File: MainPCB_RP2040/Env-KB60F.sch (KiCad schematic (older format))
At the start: 188 parts, among them J1 SKRKAEE020, J2 SKRKAEE020, J5 Conn_01x03_Male, U1 TLV75533PDBVR, U3 RP2040, Y1 3225_4P

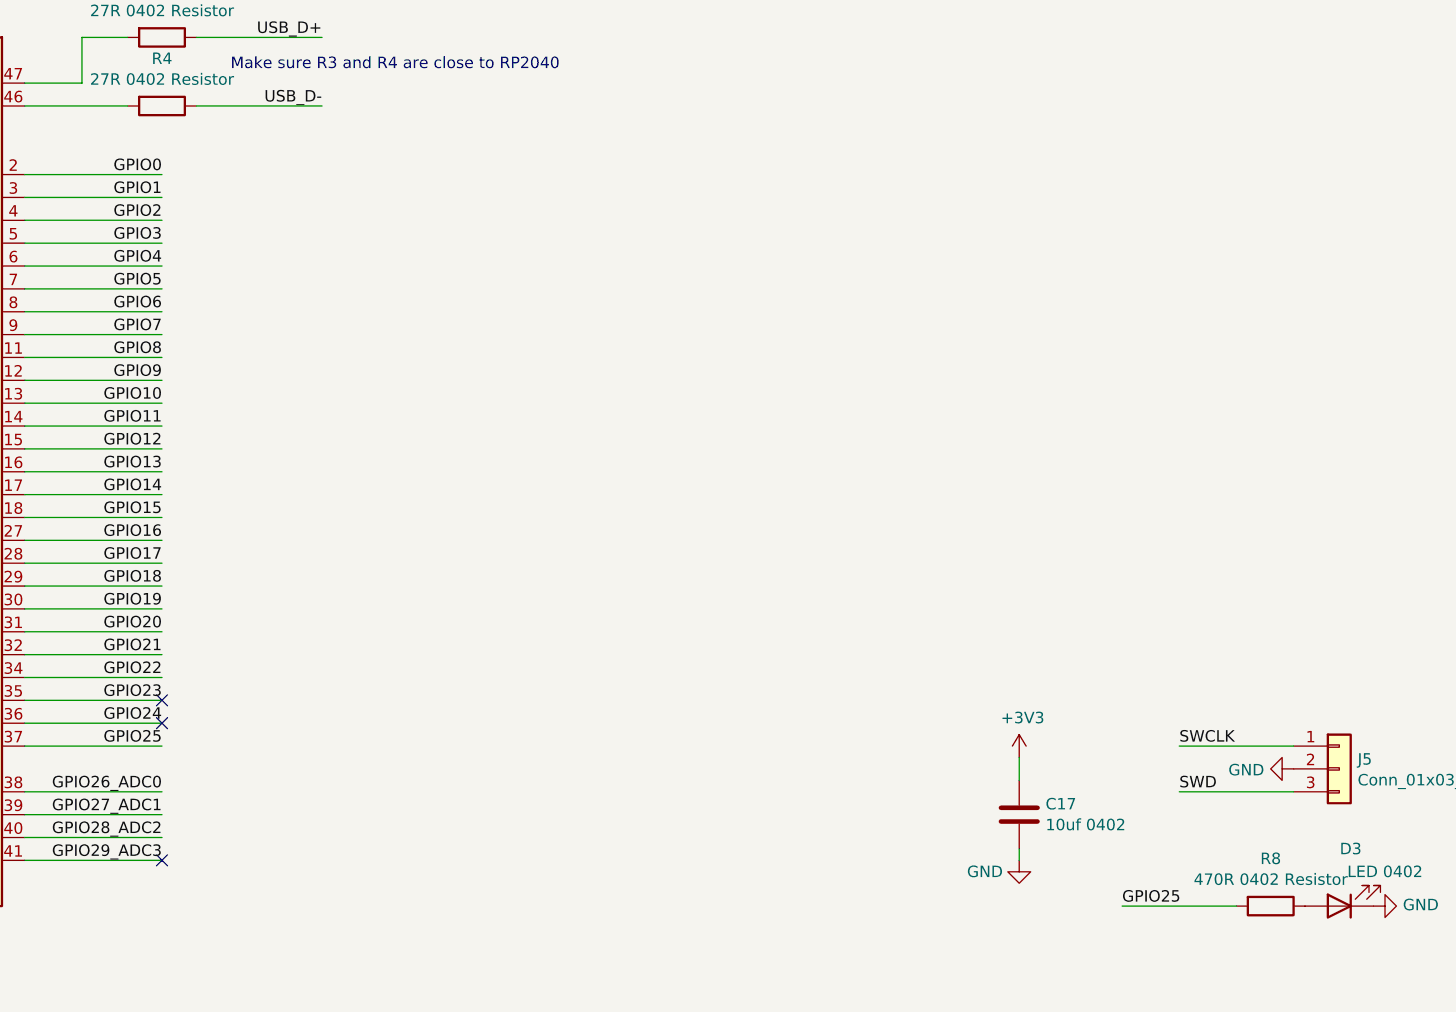
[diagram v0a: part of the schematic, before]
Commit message: finished up RP2040 version some more, added debug header and spare GPIO header.
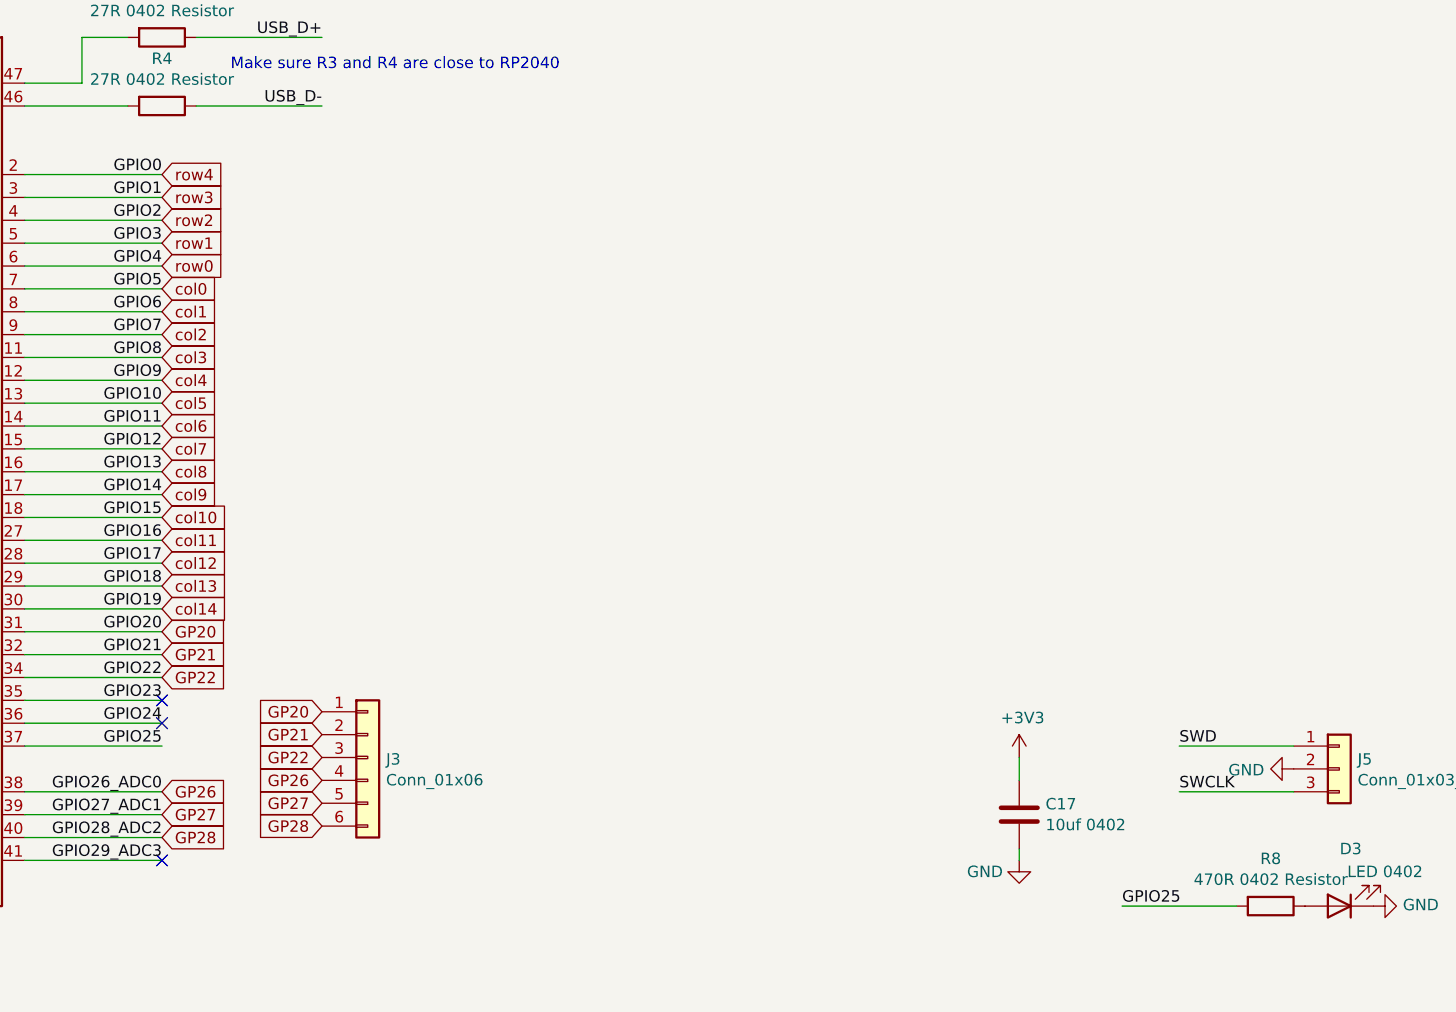
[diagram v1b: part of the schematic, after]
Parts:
- added J3: Conn_01x06, Connector_PinSocket_2.54mm:PinSocket_1x06_P2.54mm_Vertical, symbol Connector_Generic:Conn_01x06
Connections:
- net GPIO0 is gone; now on net row4: U3.2 (GPIO0)
- net GPIO1 is gone; now on net row3: U3.3 (GPIO1)
- net GPIO10 is gone; now on net col5: U3.13 (GPIO10)
- net GPIO11 is gone; now on net col6: U3.14 (GPIO11)
- net GPIO12 is gone; now on net col7: U3.15 (GPIO12)
- net GPIO13 is gone; now on net col8: U3.16 (GPIO13)
- net GPIO14 is gone; now on net col9: U3.17 (GPIO14)
- net GPIO15 is gone; now on net col10: U3.18 (GPIO15)
- net GPIO16 is gone; now on net col11: U3.27 (GPIO16)
- net GPIO17 is gone; now on net col12: U3.28 (GPIO17)
- net GPIO18 is gone; now on net col13: U3.29 (GPIO18)
- net GPIO19 is gone; now on net col14: U3.30 (GPIO19)
- net GPIO2 is gone; now on net row2: U3.4 (GPIO2)
- net GPIO3 is gone; now on net row1: U3.5 (GPIO3)
- net GPIO4 is gone; now on net row0: U3.6 (GPIO4)
- net GPIO5 is gone; now on net col0: U3.7 (GPIO5)
- net GPIO6 is gone; now on net col1: U3.8 (GPIO6)
- net GPIO7 is gone; now on net col2: U3.9 (GPIO7)
- net GPIO8 is gone; now on net col3: U3.11 (GPIO8)
- net GPIO9 is gone; now on net col4: U3.12 (GPIO9)
- net SWCLK: now also J5.3 (Pin_3); no longer J5.1 (Pin_1)
- net SWD: now also J5.1 (Pin_1); no longer J5.3 (Pin_3)
- net GPIO20 renamed GP20
- net GP20: now also J3.1 (Pin_1)
- net GPIO21 renamed GP21
- net GP21: now also J3.2 (Pin_2)
- net GPIO22 renamed GP22
- net GP22: now also J3.3 (Pin_3)
- net GPIO26_ADC0 renamed GP26
- net GP26: now also J3.4 (Pin_4)
- net GPIO27_ADC1 renamed GP27
- net GP27: now also J3.5 (Pin_5)
- net GPIO28_ADC2 renamed GP28
- net GP28: now also J3.6 (Pin_6)
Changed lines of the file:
@@
 	1    0    0    -1
 $EndComp
-Text Label 14100 7100 0    50   ~ 0
+Text Label 14100 6900 0    50   ~ 0
 SWD
 Wire Wire Line
-	14100 7100 14600 7100
+	14100 6900 14600 6900
 $Comp
 L power:GND #PWR034
@@
 $EndComp
 Wire Wire Line
-	14600 6900 14100 6900
-Text Label 14100 6900 0    50   ~ 0
+	14600 7100 14100 7100
+Text Label 14100 7100 0    50   ~ 0
 SWCLK
 Text Label 2150 4950 0    50   ~ 0
@@
 	0    1    1    0
 $EndComp
+Text GLabel 9650 4400 2    50   Input ~ 0
+row4
+Text GLabel 9650 4600 2    50   Input ~ 0
+row2
+Text GLabel 9650 4700 2    50   Input ~ 0
+row1
+Text GLabel 9650 4800 2    50   Input ~ 0
+row0
+Text GLabel 9650 4500 2    50   Input ~ 0
+row3
+Text GLabel 9650 4900 2    50   Input ~ 0
+col0
+Text GLabel 9650 5000 2    50   Input ~ 0
+col1
+Text GLabel 9650 5100 2    50   Input ~ 0
+col2
+Text GLabel 9650 5200 2    50   Input ~ 0
+col3
+Text GLabel 9650 5300 2    50   Input ~ 0
+col4
+Text GLabel 9650 5400 2    50   Input ~ 0
+col5
+Text GLabel 9650 5500 2    50   Input ~ 0
+col6
+Text GLabel 9650 5600 2    50   Input ~ 0
+col7
+Text GLabel 9650 5700 2    50   Input ~ 0
+col8
+Text GLabel 9650 5800 2    50   Input ~ 0
+col9
+Text GLabel 9650 5900 2    50   Input ~ 0
+col10
+Text GLabel 9650 6000 2    50   Input ~ 0
+col11
+Text GLabel 9650 6100 2    50   Input ~ 0
+col12
+Text GLabel 9650 6200 2    50   Input ~ 0
+col13
+Text GLabel 9650 6300 2    50   Input ~ 0
+col14
+$Comp
+L Connector_Generic:Conn_01x06 J3
+U 1 1 613572DC
+P 10550 6950
+F 0 "J3" H 10630 6942 50  0000 L CNN
+F 1 "Conn_01x06" H 10630 6851 50  0000 L CNN
+F 2 "Connector_PinSocket_2.54mm:PinSocket_1x06_P2.54mm_Vertical" H 10550 6950 50  0001 C CNN
+F 3 "~" H 10550 6950 50  0001 C CNN
+	1    10550 6950
+	1    0    0    -1
+$EndComp
+Text GLabel 10350 6750 0    50   Input ~ 0
+GP20
+Text GLabel 10350 6850 0    50   Input ~ 0
+GP21
+Text GLabel 10350 6950 0    50   Input ~ 0
+GP22
+Text GLabel 10350 7050 0    50   Input ~ 0
+GP26
+Text GLabel 10350 7150 0    50   Input ~ 0
+GP27
+Text GLabel 10350 7250 0    50   Input ~ 0
+GP28
+Text GLabel 9650 6400 2    50   Input ~ 0
+GP20
+Text GLabel 9650 6500 2    50   Input ~ 0
+GP21
+Text GLabel 9650 6600 2    50   Input ~ 0
+GP22
+Text GLabel 9650 7100 2    50   Input ~ 0
+GP26
+Text GLabel 9650 7200 2    50   Input ~ 0
+GP27
+Text GLabel 9650 7300 2    50   Input ~ 0
+GP28
 $EndSCHEMATC

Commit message: Corrected mount hole placement on all PCBs and updated the switch plate to fit triple spacebar split.
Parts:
- H2, H4, H6: symbol Mechanical:MountingHole -> Mechanical:MountingHole_Pad
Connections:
- net GND: now also H2.1, H4.1, H6.1
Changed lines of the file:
@@
 $EndComp
 $Comp
-L Mechanical:MountingHole H2
+L Mechanical:MountingHole_Pad H2
 U 1 1 609389EF
-P 22900 8600
-F 0 "H2" H 23000 8646 50  0000 L CNN
-F 1 "MountingHole" H 23000 8555 50  0000 L CNN
-F 2 "AKLogo:MountingHole_2.2mm_M2-MODIFIED" H 22900 8600 50  0001 C CNN
-F 3 "~" H 22900 8600 50  0001 C CNN
-	1    22900 8600
-	1    0    0    -1
-$EndComp
-$Comp
-L Mechanical:MountingHole H4
+P 22100 8100
+F 0 "H2" H 22200 8146 50  0000 L CNN
+F 1 "MountingHole" H 22200 8055 50  0000 L CNN
+F 2 "AKLogo:MountingHole_2.2mm_M2-MODIFIED" H 22100 8100 50  0001 C CNN
+F 3 "~" H 22100 8100 50  0001 C CNN
+	1    22100 8100
+	0    1    1    0
+$EndComp
+$Comp
+L Mechanical:MountingHole_Pad H4
 U 1 1 609389F5
-P 22900 8800
-F 0 "H4" H 23000 8846 50  0000 L CNN
-F 1 "MountingHole" H 23000 8755 50  0000 L CNN
-F 2 "AKLogo:MountingHole_2.2mm_M2-MODIFIED" H 22900 8800 50  0001 C CNN
-F 3 "~" H 22900 8800 50  0001 C CNN
-	1    22900 8800
-	1    0    0    -1
-$EndComp
-$Comp
-L Mechanical:MountingHole H6
+P 22100 8300
+F 0 "H4" H 22200 8346 50  0000 L CNN
+F 1 "MountingHole" H 22200 8255 50  0000 L CNN
+F 2 "AKLogo:MountingHole_2.2mm_M2-MODIFIED" H 22100 8300 50  0001 C CNN
+F 3 "~" H 22100 8300 50  0001 C CNN
+	1    22100 8300
+	0    1    1    0
+$EndComp
+$Comp
+L Mechanical:MountingHole_Pad H6
 U 1 1 609389FB
-P 22900 9000
-F 0 "H6" H 23000 9046 50  0000 L CNN
-F 1 "MountingHole" H 23000 8955 50  0000 L CNN
-F 2 "AKLogo:MountingHole_2.2mm_M2-MODIFIED" H 22900 9000 50  0001 C CNN
-F 3 "~" H 22900 9000 50  0001 C CNN
-	1    22900 9000
-	1    0    0    -1
+P 22100 8500
+F 0 "H6" H 22200 8546 50  0000 L CNN
+F 1 "MountingHole" H 22200 8455 50  0000 L CNN
+F 2 "AKLogo:MountingHole_2.2mm_M2-MODIFIED" H 22100 8500 50  0001 C CNN
+F 3 "~" H 22100 8500 50  0001 C CNN
+	1    22100 8500
+	0    1    1    0
 $EndComp
 $Comp
@@
 Text GLabel 9650 7300 2    50   Input ~ 0
 GP28
+Wire Wire Line
+	22000 8600 22000 8500
+Connection ~ 22000 8600
+Wire Wire Line
+	22000 8500 22000 8300
+Connection ~ 22000 8500
+Wire Wire Line
+	22000 8300 22000 8100
+Connection ~ 22000 8300
 $EndSCHEMATC
